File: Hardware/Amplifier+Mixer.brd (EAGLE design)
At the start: 140 x 140 mm, 193 parts, among them IC1 7812, IC2 7805, IC3 7912, IC4 OPA134PA, IC5 OPA134PA, IC6 MEGA8-AI, IC7 74HCT04, IC8 LM358D, IC9 LM358D, J1 6MM, J10 JST-XH2, J2 6MM, J3 6MM, J4 6MM, J5 TERMINAL-BLOCK-2PLUG-IN, J6 TERMINAL-BLOCK-2PLUG-IN, J7 ENCODER, J8 DISPLAY, J9 USB, K1 12V 8A, K2 12V 8A, T1 BC817, T2 BC817, T3 BC817, T4 BC817, U1 LM1117-3.3, U2 10k, U3 10k, U4 10k, U5 10k, U6 TDA7498L, U7 10k, U8 10k, U9 MCP9700SMD, X1 RCA-4-CHANNEL, X2 JST-XH2, X3 ICSP

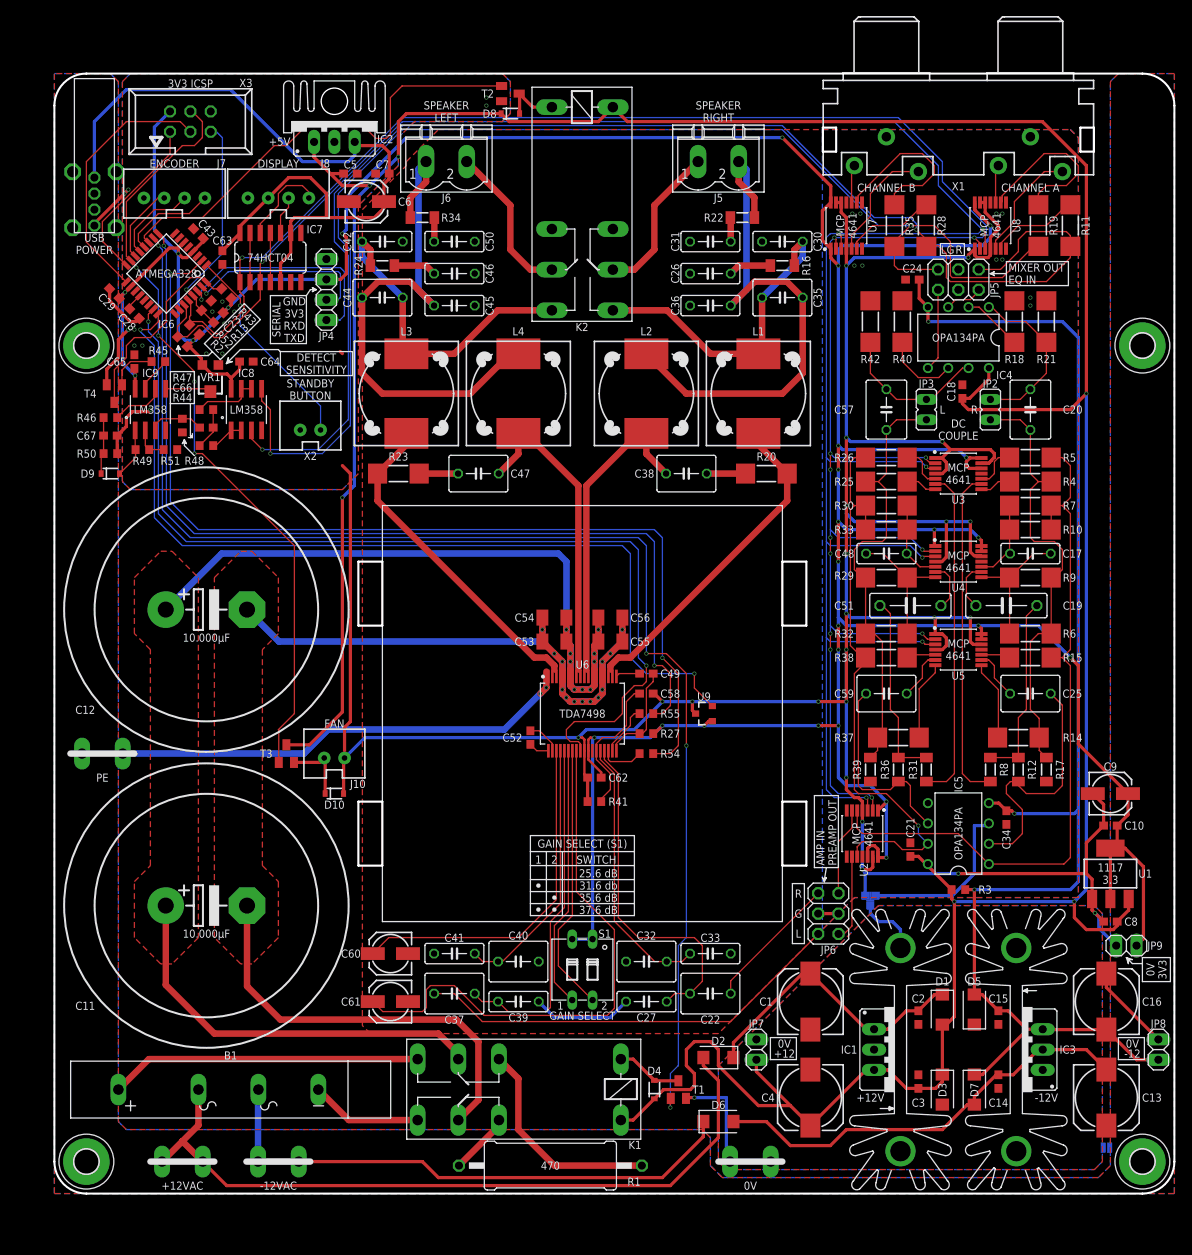
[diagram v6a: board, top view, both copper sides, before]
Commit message: added power led connector
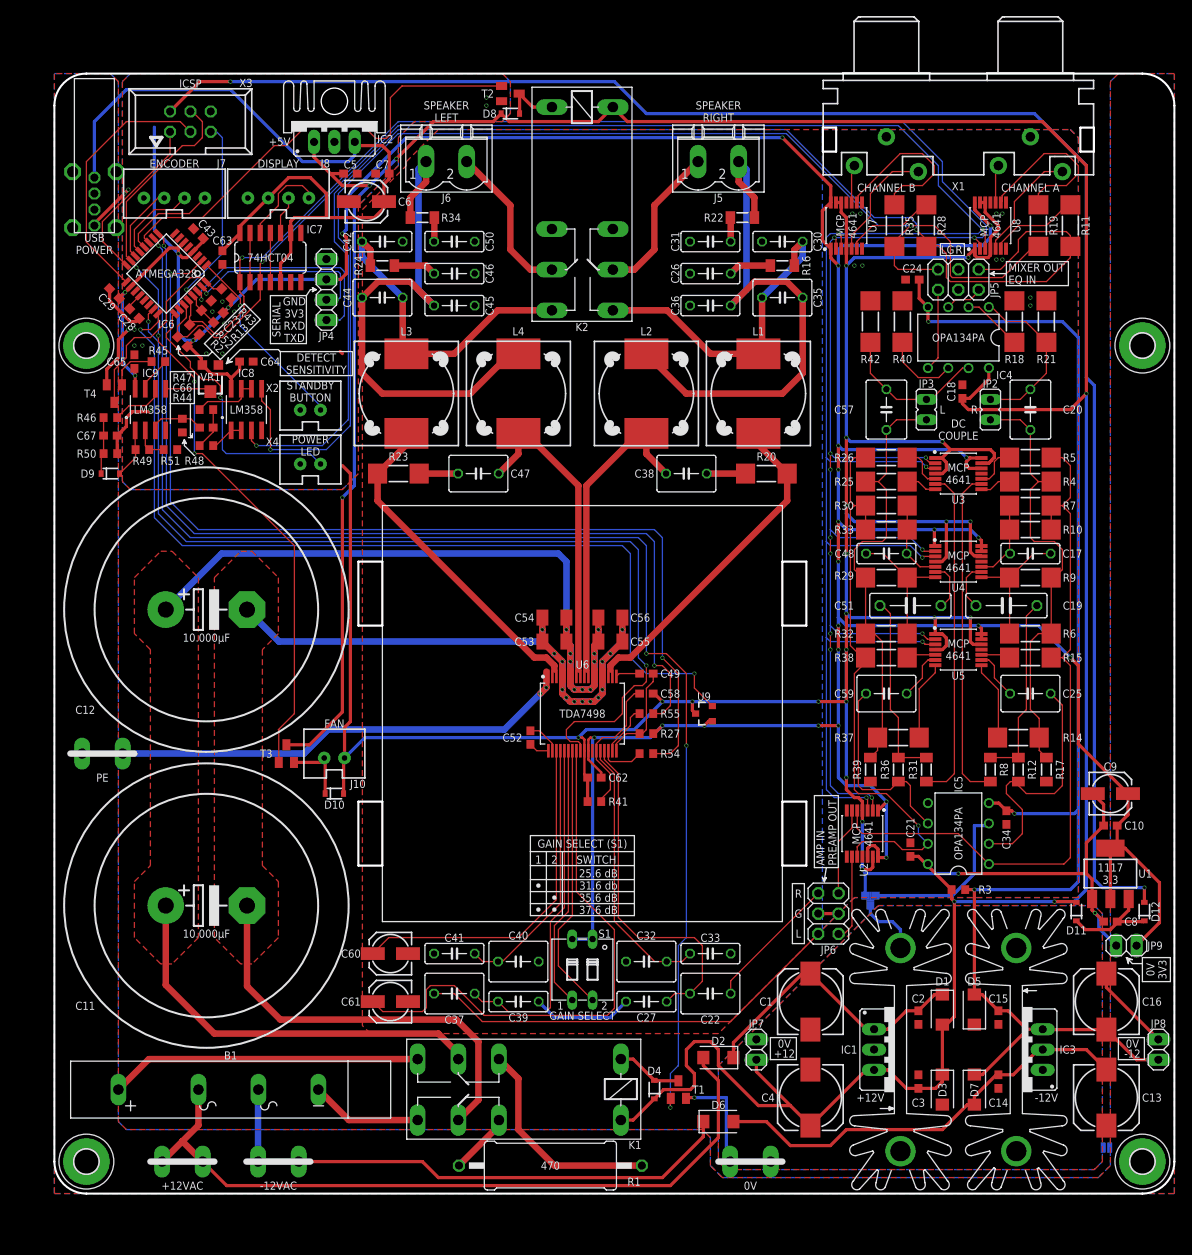
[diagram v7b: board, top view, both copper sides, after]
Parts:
- added D11, D12: 1N4148, SparkFun-DiscreteSemi:SOD-323
- added X4: JST-XH2, Class D Amp:JST-2-PTH-VERT
- moved X2 2.50 mm to (32.0, 98.5)
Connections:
- new net N$57: C8.1, D11.C, D12.C, U1.3
- new net POWER_LED: IC6.25, X4.2
- new net VPP: D12.A, X3.2
- net +12V: now also D11.A; no longer C8.1, U1.3
- net +3V3: no longer X3.2
- net DGND: now also X4.1
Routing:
- net VPP: track 0.00 -> 218.6 mm, vias 0 -> 2
- net POWER_LED: track 0.00 -> 34.2 mm, vias 0 -> 1
- net N$57: track 0.00 -> 12.9 mm
- net +12V: track 428.5 -> 416.6 mm
- net PWR_BTN: track 26.5 -> 24.0 mm
- net MIX_L: track 163.7 -> 162.6 mm
- net +3V3: track 493.9 -> 492.8 mm
- net MIX_R: track 169.1 -> 168.4 mm
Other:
- board text added: "ICSP"
- board text added: "POWER LED"
- board text removed: "3V3 ICSP"

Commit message: removed 74hct04 for level shifting
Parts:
- removed IC7: 74HCT04, 74xx-eu:SO14
- removed R43: 10k, rcl:R0603
- removed T4: BC817, transistor:SOT23-BEC
- moved C63 4.12 mm to (22.0, 121.0), turned to 0 degrees
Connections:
- removed net N$37: R45.1, T4.B
- removed net N$60: IC7.13, IC7.2
- removed net N$83: IC7.11, IC7.4
- removed net SCL_5V: IC7.12, J8.4
- removed net SDA_5V: IC7.10, J8.3
- net +3V3: no longer R43.1
- net +5V: no longer IC7.14, IC7.5, IC7.9
- net AUDIO_DETECT: now also R45.1; no longer R43.2, T4.C
- net DGND: no longer IC7.7, T4.E
- net SCL: now also J8.4; no longer IC7.1
- net SDA: now also J8.3; no longer IC7.3
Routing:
- net +3V3: track 492.8 -> 474.4 mm
- net +5V: track 100.6 -> 83.6 mm
- net SCL_5V: track 11.2 -> 0.00 mm
- net AUDIO_DETECT: track 25.2 -> 14.8 mm
- net SCL: track 267.2 -> 276.7 mm
- net DGND: track 409.3 -> 401.3 mm, vias 37 -> 36
- net N$83: track 6.15 -> 0.00 mm
- net N$60: track 6.15 -> 0.00 mm
- net N$37: track 5.98 -> 0.00 mm
- net SDA: track 270.1 -> 275.4 mm
- net SDA_5V: track 4.79 -> 0.00 mm
